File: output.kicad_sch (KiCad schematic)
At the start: 31 parts, among them J1 SMA, J2 SMA, J3 SMA, J4 SMA, J5 U.Fl, T1 MABA-007159-000000, T2 MABA-007159-000000, U31 TLV3601DCKR, U32 TLV3601DCKR

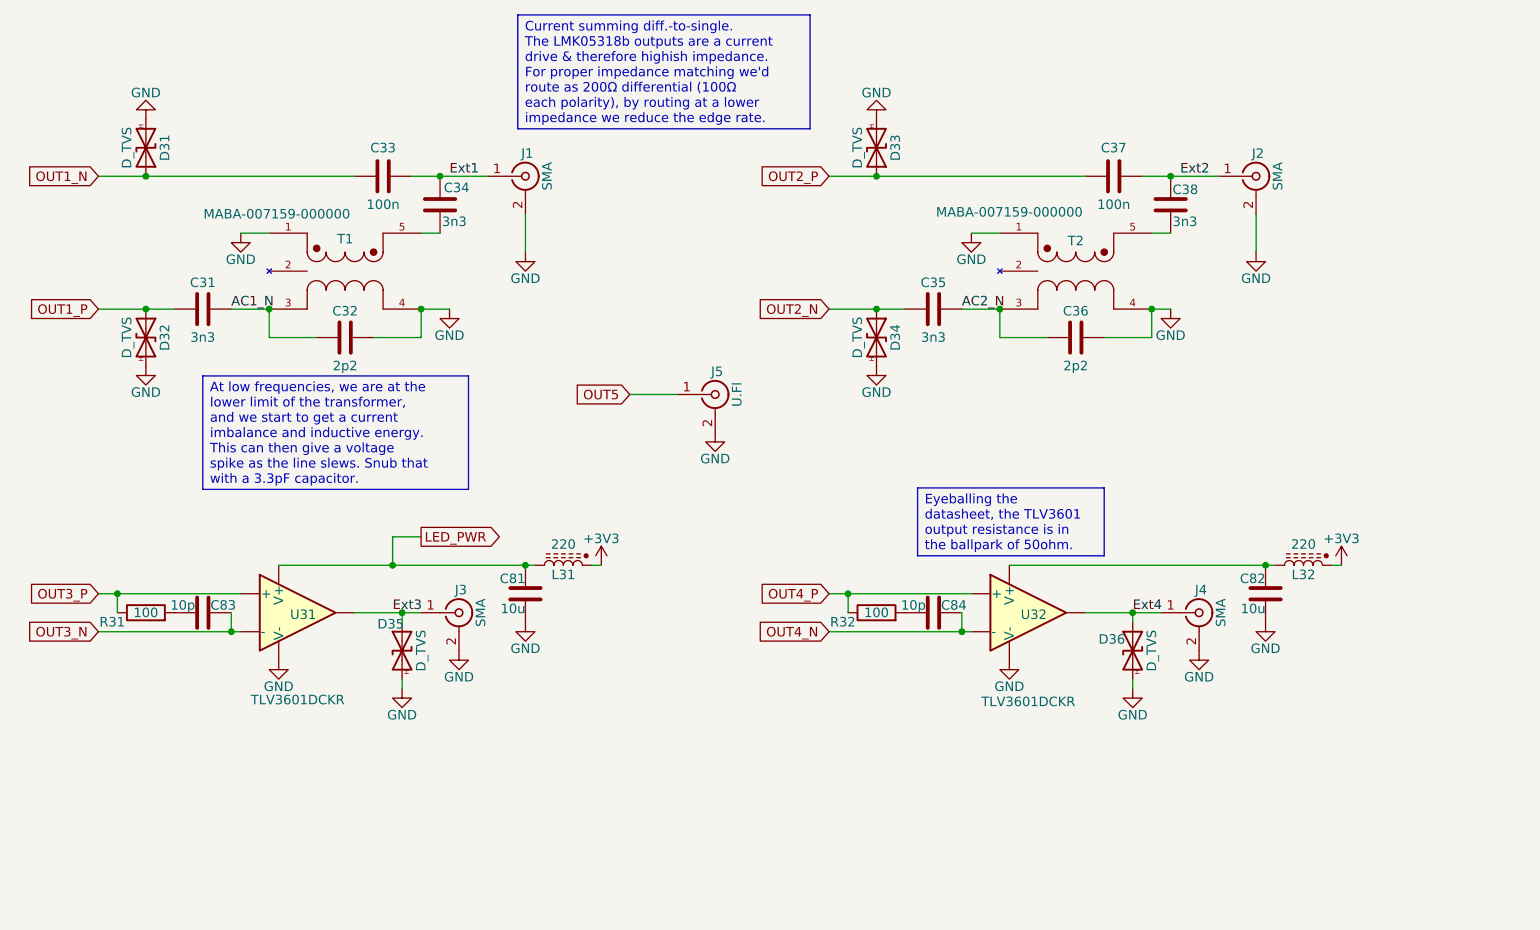
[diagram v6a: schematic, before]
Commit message: Use impedance matching baluns.
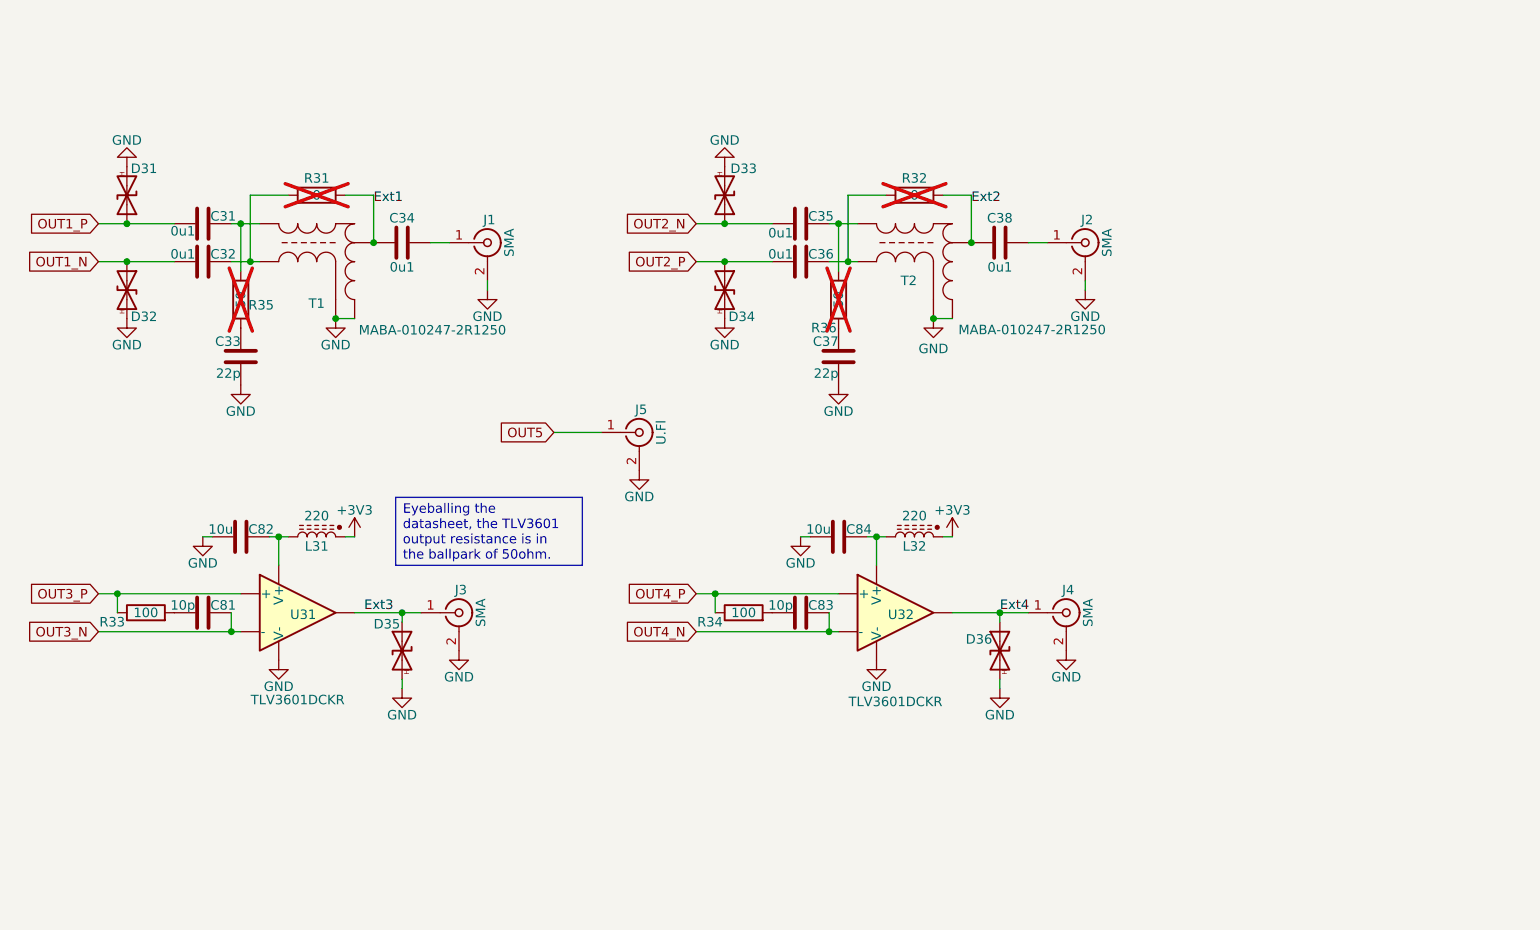
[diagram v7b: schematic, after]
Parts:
- added R31, R32: 0, Resistor_SMD:R_0603_1608Metric, symbol Device:R
- added R35, R36: 50, Resistor_SMD:R_0603_1608Metric, symbol Device:R
- C31, C35: value 3n3 -> 0u1
- C32, C36: value 2p2 -> 0u1
- C33, C37: value 100n -> 22p; LCSC (none) -> C32949
- C34, C38: value 3n3 -> 0u1; LCSC C26404 -> (none)
- T1, T2: value MABA-007159-000000 -> MABA-010247-2R1250; symbol Parts:MABA-007159-000000 -> Parts:MABA-010247-2R1250; LCSC C350943 -> (none)
- renumbered C83 to C81, C81 to C82, C84 to C83, C82 to C84, R31 to R33, R32 to R34
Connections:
- net Ext1: now also C34.1, T1.4, R31.2; no longer C33.2, C34.2, J1.1 (In)
- net Ext2: now also C38.1, T2.4, R32.2; no longer C37.2, C38.2, J2.1 (In)
- net GND: now also C33.1, C37.1, T1.2, T1.5, T2.2, T2.5; no longer C32.2, C36.2, T1.1, T1.4, T2.1, T2.4
- net OUT1_N: now also C32.1, D32.1 (A1); no longer C33.1, D31.1 (A1)
- net OUT1_P: now also D31.1 (A1); no longer D32.1 (A1)
- net OUT2_N: now also D33.1 (A1); no longer D34.1 (A1)
- net OUT2_P: now also C36.1, D34.1 (A1); no longer C37.1, D33.1 (A1)
- removed net AC1_N: C31.2, C32.1, T1.3
- removed net AC2_N: C35.2, C36.1, T2.3
- net LED_PWR: no longer names the net of C82.1, L31.2, U31.5 (V+)
- new net: C32.2, R31.1, T1.3
- new net: C36.2, R32.1, T2.3
- new net: C37.2, R36.1
- new net: C35.2, R36.2, T2.1
- new net: C33.2, R35.1
- new net: C31.2, R35.2, T1.1
- new net: C34.2, J1.1 (In)
- new net: C38.2, J2.1 (In)
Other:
- moved on the sheet: C31, C82, C83, C84, D31, D32, D33, D34, D36, J1, J2, J4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

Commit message: Routing basically done.
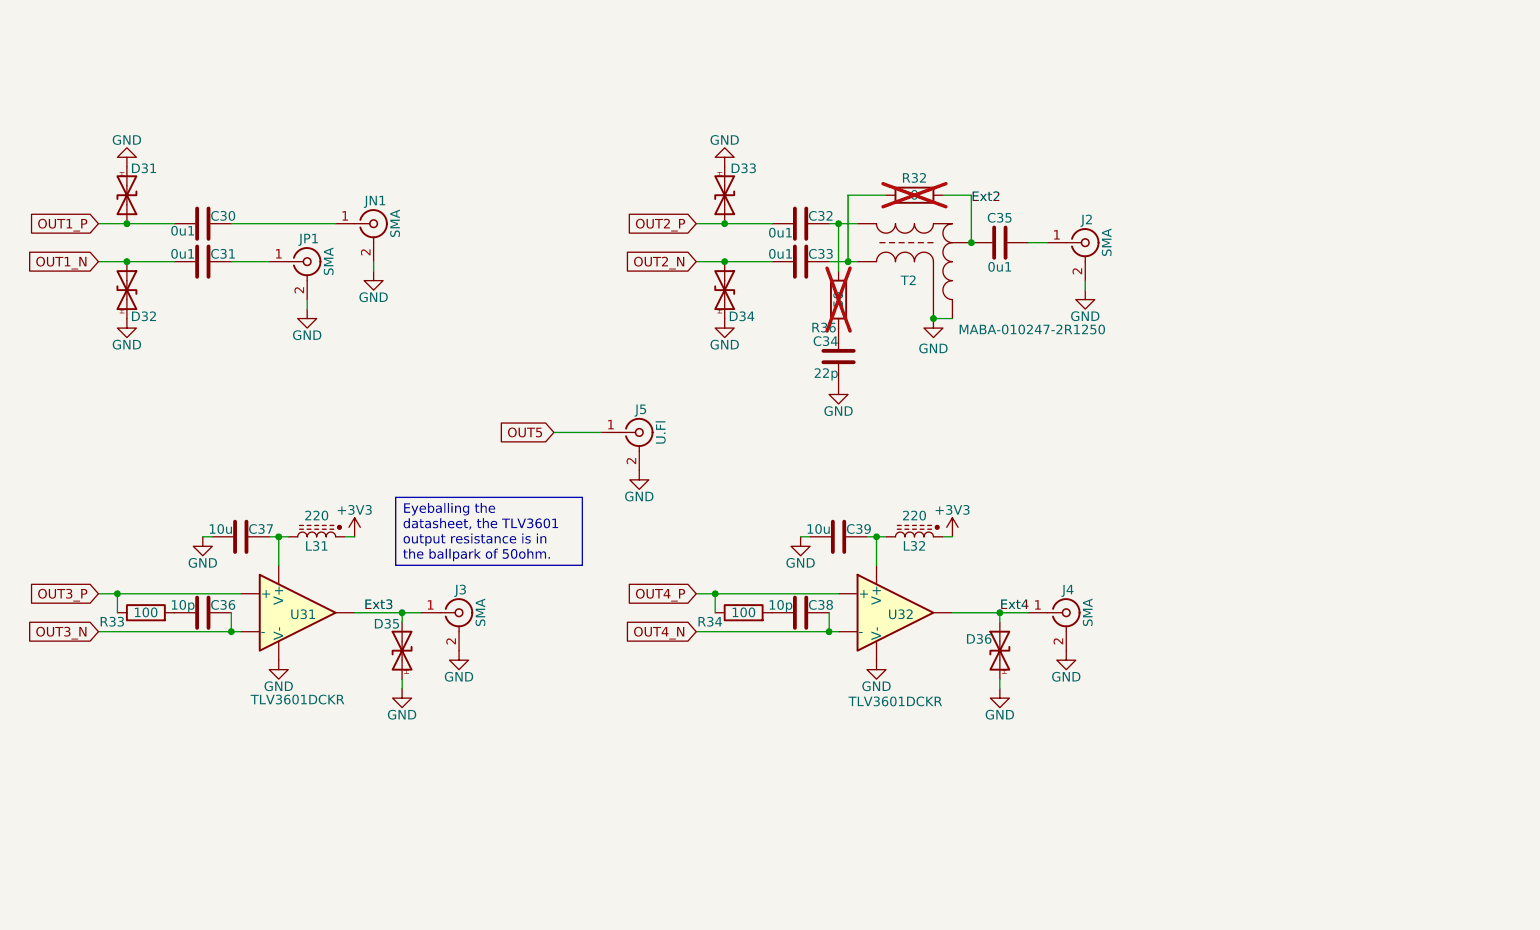
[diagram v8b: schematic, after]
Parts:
- removed C33: 22p, Capacitor_SMD:C_0402_1005Metric, symbol Device:C
- removed C34: 0u1, Capacitor_SMD:C_0402_1005Metric, symbol Device:C
- removed R31: 0, Resistor_SMD:R_0603_1608Metric, symbol Device:R
- removed R35: 50, Resistor_SMD:R_0603_1608Metric, symbol Device:R
- removed T1: MABA-010247-2R1250, Parts:XFMR_MABA-007159-000000, symbol Parts:MABA-010247-2R1250
- added JN1: SMA, Parts:SMA_EdgeMount, symbol Connector:Conn_Coaxial
- renumbered C31 to C30, C32 to C31, C35 to C32, C36 to C33, C37 to C34, C38 to C35, C81 to C36, C82 to C37, C83 to C38, C84 to C39, J1 to JP1
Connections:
- net GND: now also JN1.2 (Ext)
- net OUT2_N: now also C33.1, D34.1 (A1); no longer C32.1, D33.1 (A1)
- net OUT2_P: now also C32.1, D33.1 (A1); no longer C33.1, D34.1 (A1)
- net at C31.2: now also JP1.1 (In)
- net at C30.2: now also JN1.1 (In)
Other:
- moved on the sheet: JP1
